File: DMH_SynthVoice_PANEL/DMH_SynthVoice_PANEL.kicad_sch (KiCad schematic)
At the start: 5 parts, among them J0 Panel_GND_Solder_Wire_Pad

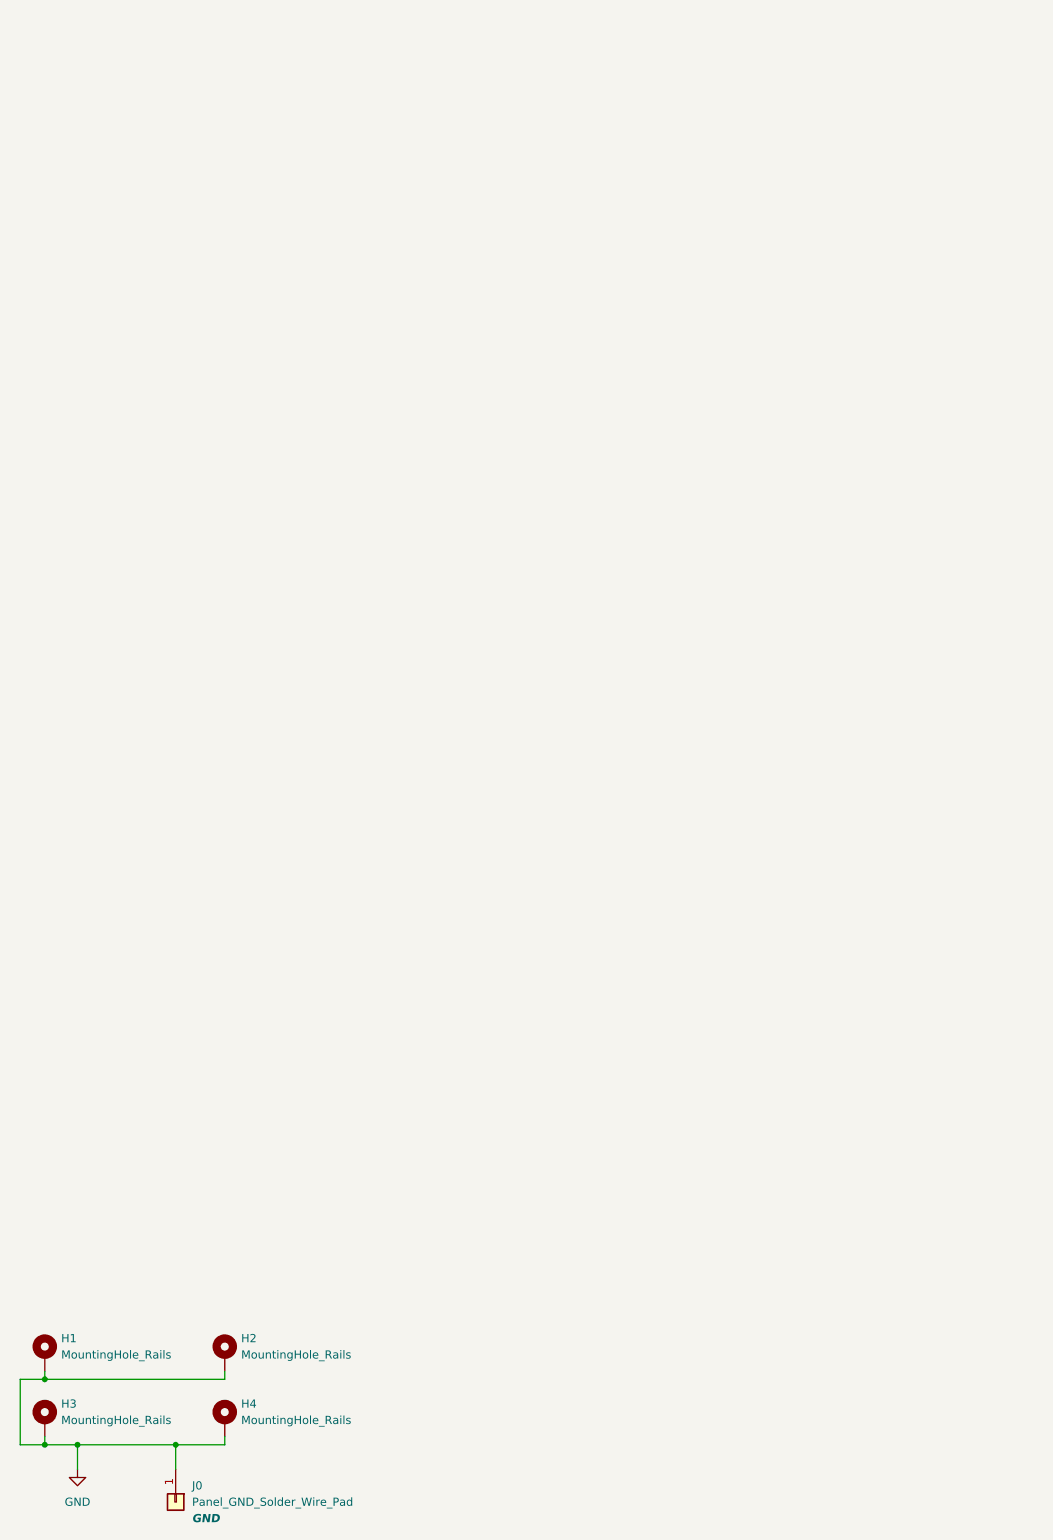
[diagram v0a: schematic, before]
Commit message: Designed front panel
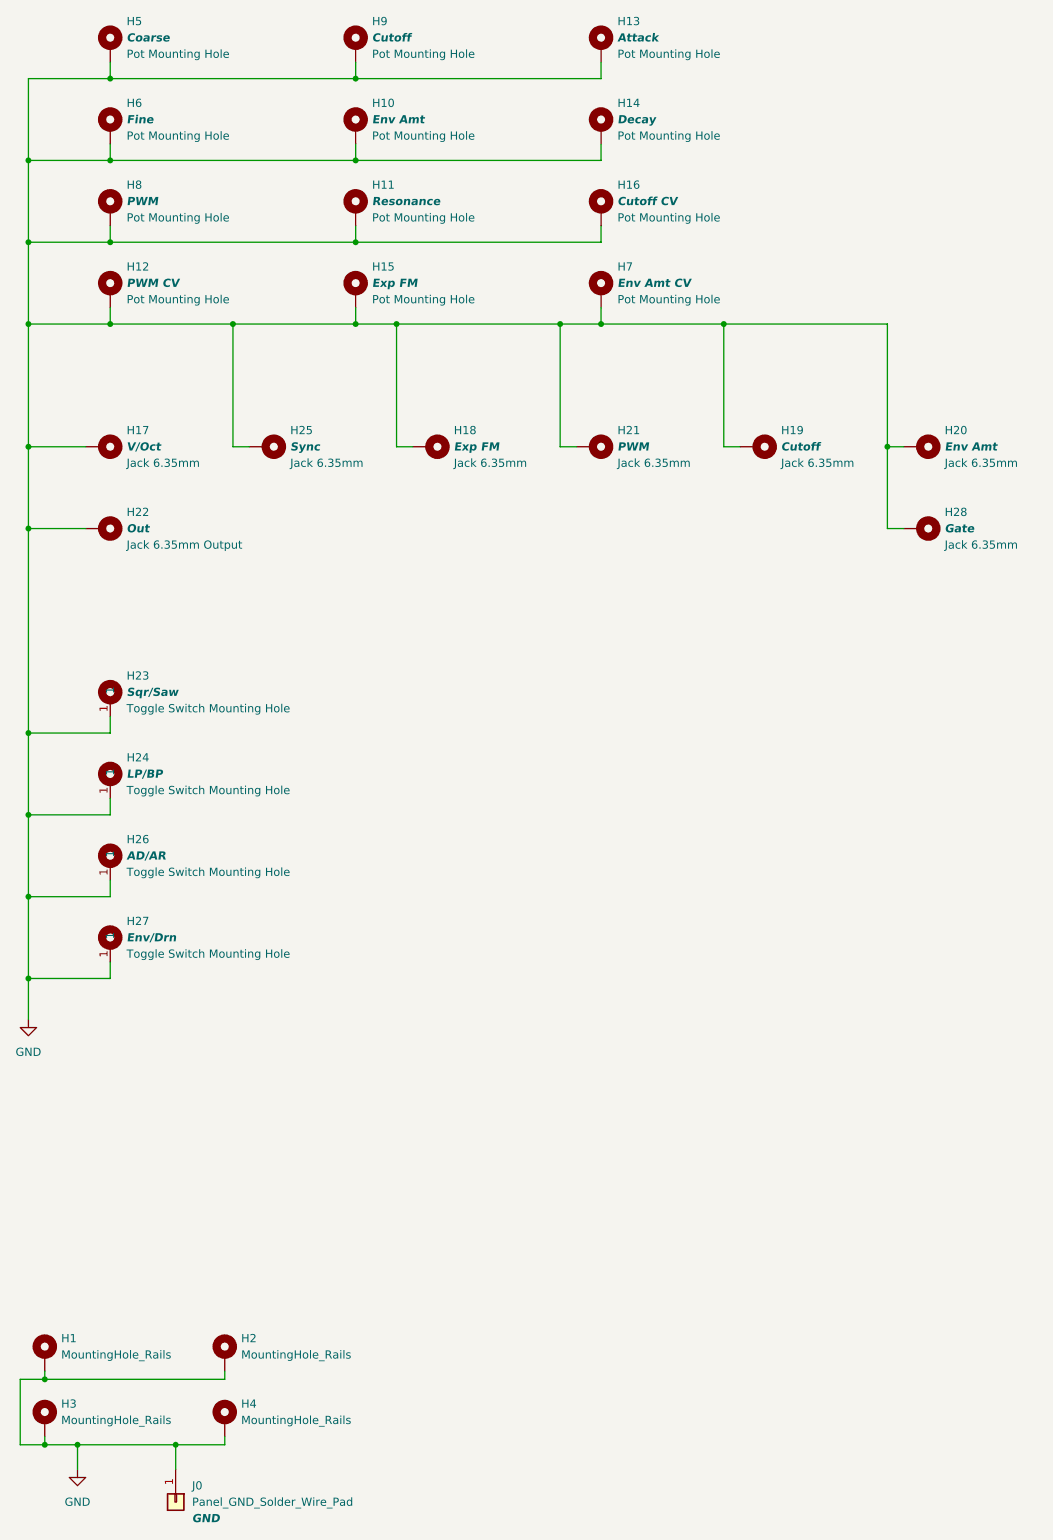
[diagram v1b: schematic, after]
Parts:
- added H10: Env Amt, SynthStuff:Pot_Cutout_Tiny_attv_P110KH1, symbol SynthStuff:MountingHole_Pot
- added H11: Resonance, SynthStuff:Pot_Cutout_Small, symbol SynthStuff:MountingHole_Pot
- added H12: PWM CV, SynthStuff:Pot_Cutout_Tiny_attv_P110KH1, symbol SynthStuff:MountingHole_Pot
- added H13: Attack, SynthStuff:Pot_Cutout_Small, symbol SynthStuff:MountingHole_Pot
- added H14: Decay, SynthStuff:Pot_Cutout_Small, symbol SynthStuff:MountingHole_Pot
- added H15: Exp FM, SynthStuff:Pot_Cutout_Tiny_attv_P110KH1, symbol SynthStuff:MountingHole_Pot
- added H16: Cutoff CV, SynthStuff:Pot_Cutout_Tiny_attv_P110KH1, symbol SynthStuff:MountingHole_Pot
- added H17: V/Oct, SynthStuff:Jack_6.35mm_Cutout_v3, symbol SynthStuff:MountingHole_Jack6.35mm_v2
- added H18: Exp FM, SynthStuff:Jack_6.35mm_Cutout_v3, symbol SynthStuff:MountingHole_Jack6.35mm_v2
- added H19: Cutoff, SynthStuff:Jack_6.35mm_Cutout_v3, symbol SynthStuff:MountingHole_Jack6.35mm_v2
- added H20: Env Amt, SynthStuff:Jack_6.35mm_Cutout_v3, symbol SynthStuff:MountingHole_Jack6.35mm_v2
- added H21: PWM, SynthStuff:Jack_6.35mm_Cutout_v3, symbol SynthStuff:MountingHole_Jack6.35mm_v2
- added H22: Out, SynthStuff:Jack_6.35mm_Cutout_Output_v6, symbol SynthStuff:MountingHole_Jack6.35mm_Output_v2
- added H23: Sqr/Saw, SynthStuff:Toggle_Switch_TE_Cutout, symbol SynthStuff:MountingHole_ToggleSwitch
- added H24: LP/BP, SynthStuff:Toggle_Switch_TE_Cutout, symbol SynthStuff:MountingHole_ToggleSwitch
- added H25: Sync, SynthStuff:Jack_6.35mm_Cutout_v3, symbol SynthStuff:MountingHole_Jack6.35mm_v2
- added H26: AD/AR, SynthStuff:Toggle_Switch_TE_Cutout, symbol SynthStuff:MountingHole_ToggleSwitch
- added H27: Env/Drn, SynthStuff:Toggle_Switch_TE_Cutout, symbol SynthStuff:MountingHole_ToggleSwitch
- added H28: Gate, SynthStuff:Jack_6.35mm_Cutout_v3, symbol SynthStuff:MountingHole_Jack6.35mm_v2
- added H5: Coarse, SynthStuff:Pot_Cutout_Small, symbol SynthStuff:MountingHole_Pot
- added H6: Fine, SynthStuff:Pot_Cutout_Small, symbol SynthStuff:MountingHole_Pot
- added H7: Env Amt CV, SynthStuff:Pot_Cutout_Tiny_attv_P110KH1, symbol SynthStuff:MountingHole_Pot
- added H8: PWM, SynthStuff:Pot_Cutout_Small, symbol SynthStuff:MountingHole_Pot
- added H9: Cutoff, SynthStuff:Pot_Cutout_Small, symbol SynthStuff:MountingHole_Pot
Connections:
- net GND: now also H10.1, H11.1, H12.1, H13.1, H14.1, H15.1, H16.1, H17.1, H18.1, H19.1, H20.1, H21.1, H22.1, H23.1, H24.1, H25.1, H26.1, H27.1, H28.1, H5.1, H6.1, H7.1, H8.1, H9.1

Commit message: Matched panel layout to SuperSaw module
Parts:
- H10: value Env Amt -> F.E. Amt; footprint SynthStuff:Pot_Cutout_Tiny_attv_P110KH1 -> SynthStuff:Pot_Cutout_Small_attv_P110KH1
- H11: value Resonance -> Cutoff
- H13: value Attack -> Decay
- H14: value Decay -> Resonance
- H15: value Exp FM -> Cutoff CV
- H16: value Cutoff CV -> Exp FM CV
- H20: value Env Amt -> F.E. Amt
- H24: value LP/BP -> AD/AR
- H26: value AD/AR -> LP/BP
- H27: value Env/Drn -> A.E +/d/-
- H7: value Env Amt CV -> F.E. Amt CV
- H9: value Cutoff -> Attack
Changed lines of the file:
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@@
 			)
 		)
-		(property "Value" "LP/BP"
+		(property "Value" "AD/AR"
 			(at 40.64 165.1 0)
 			(effects
@@
 			)
 		)
-		(property "Value" "AD/AR"
+		(property "Value" "LP/BP"
 			(at 40.64 177.8 0)
 			(effects
@@
 			)
 		)
-		(property "Value" "Exp FM"
+		(property "Value" "Cutoff CV"
 			(at 78.74 88.9 0)
 			(effects
@@
 			)
 		)
-		(property "Value" "Attack"
+		(property "Value" "Decay"
 			(at 116.84 50.8 0)
 			(effects
@@
 			)
 		)
-		(property "Value" "Env Amt CV"
+		(property "Value" "F.E. Amt CV"
 			(at 116.84 88.9 0)
 			(effects
@@
 			)
 		)
-		(property "Value" "Decay"
+		(property "Value" "Resonance"
 			(at 116.84 63.5 0)
 			(effects
@@
 			)
 		)
-		(property "Value" "Cutoff"
+		(property "Value" "Attack"
 			(at 78.74 50.8 0)
 			(effects
@@
 			)
 		)
-		(property "Value" "Resonance"
+		(property "Value" "Cutoff"
 			(at 78.74 76.2 0)
 			(effects
@@
 			)
 		)
-		(property "Value" "Env Amt"
+		(property "Value" "F.E. Amt"
 			(at 167.64 114.3 0)
 			(effects
@@
 			)
 		)
-		(property "Value" "Env/Drn"
+		(property "Value" "A.E +/d/-"
 			(at 40.64 190.5 0)
 			(effects
@@
 			)
 		)
-		(property "Value" "Env Amt"
+		(property "Value" "F.E. Amt"
 			(at 78.74 63.5 0)
 			(effects
@@
 			)
 		)
-		(property "Footprint" "SynthStuff:Pot_Cutout_Tiny_attv_P110KH1"
+		(property "Footprint" "SynthStuff:Pot_Cutout_Small_attv_P110KH1"
 			(at 76.2 64.77 0)
 			(effects
@@
 			)
 		)
-		(property "Value" "Cutoff CV"
+		(property "Value" "Exp FM CV"
 			(at 116.84 76.2 0)
 			(effects
